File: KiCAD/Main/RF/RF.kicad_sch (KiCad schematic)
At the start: 2 parts

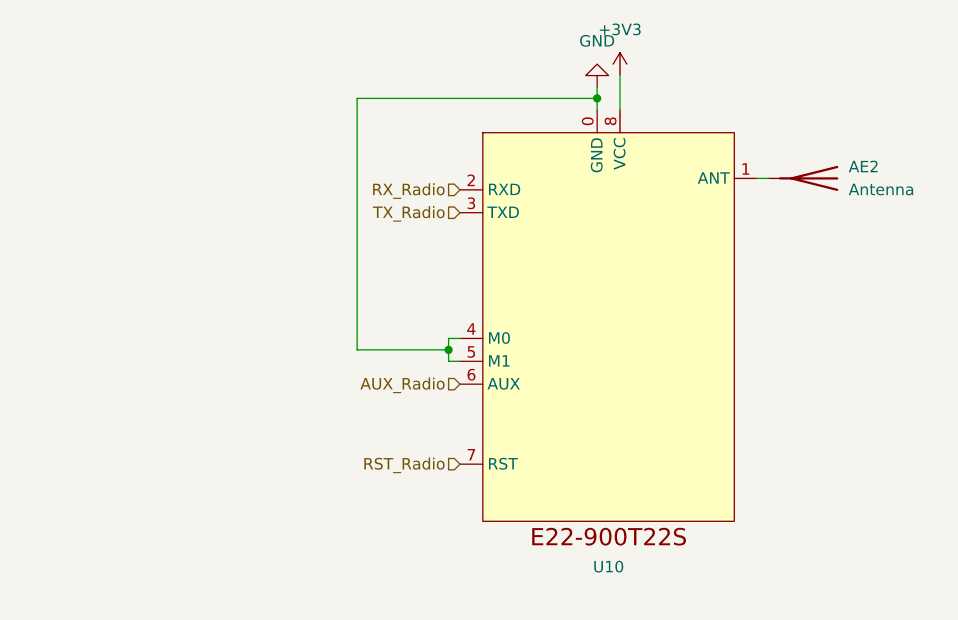
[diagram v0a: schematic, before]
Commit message: Add datasheets and revise TMR goals
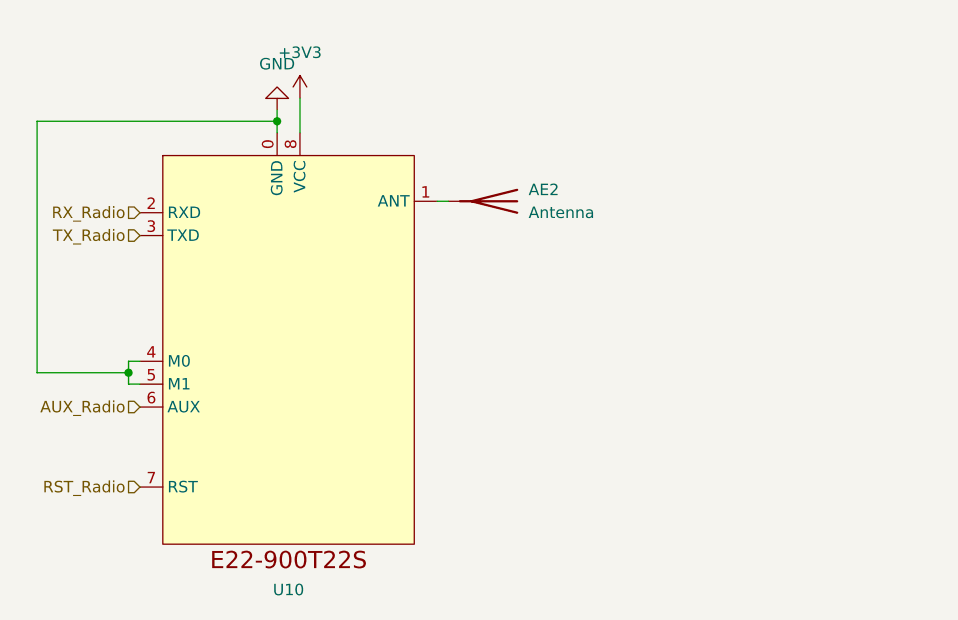
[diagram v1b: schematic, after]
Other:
- company: (none) -> Liquid Rocketry at Illinois Airframe Avionics
- title: (none) -> Ebyte E22 Radio Module
- moved on the sheet: AE2, U10
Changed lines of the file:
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@@
 	(generator_version "9.0")
 	(paper "USLetter")
+	(title_block
+		(title "Ebyte E22 Radio Module")
+		(company "Liquid Rocketry at Illinois Airframe Avionics")
+		(comment 1 "Designed by: Aleph Qin (AE, TMGT Student)")
+	)
 	(junction
-		(at 173.99 76.2)
+		(at 138.43 78.74)
 		(diameter 0)
 		(color 0 0 0 0)
 	)
 	(junction
-		(at 157.48 104.14)
+		(at 121.92 106.68)
 		(diameter 0)
 		(color 0 0 0 0)
@@
 	(wire
 		(pts
-			(xy 158.75 105.41) (xy 157.48 105.41)
-		)
-		(stroke
-			(width 0)
-			(type default)
-		)
-	)
-	(wire
-		(pts
-			(xy 157.48 105.41) (xy 157.48 104.14)
-		)
-		(stroke
-			(width 0)
-			(type default)
-		)
-	)
-	(wire
-		(pts
-			(xy 176.53 73.66) (xy 176.53 77.47)
-		)
-		(stroke
-			(width 0)
-			(type default)
-		)
-	)
-	(wire
-		(pts
-			(xy 147.32 76.2) (xy 147.32 104.14)
-		)
-		(stroke
-			(width 0)
-			(type default)
-		)
-	)
-	(wire
-		(pts
-			(xy 147.32 104.14) (xy 157.48 104.14)
-		)
-		(stroke
-			(width 0)
-			(type default)
-		)
-	)
-	(wire
-		(pts
-			(xy 193.04 85.09) (xy 191.77 85.09)
-		)
-		(stroke
-			(width 0)
-			(type default)
-		)
-	)
-	(wire
-		(pts
-			(xy 173.99 76.2) (xy 147.32 76.2)
-		)
-		(stroke
-			(width 0)
-			(type default)
-		)
-	)
-	(wire
-		(pts
-			(xy 157.48 102.87) (xy 157.48 104.14)
-		)
-		(stroke
-			(width 0)
-			(type default)
-		)
-	)
-	(wire
-		(pts
-			(xy 173.99 76.2) (xy 173.99 77.47)
-		)
-		(stroke
-			(width 0)
-			(type default)
-		)
-	)
-	(wire
-		(pts
-			(xy 173.99 74.93) (xy 173.99 76.2)
-		)
-		(stroke
-			(width 0)
-			(type default)
-		)
-	)
-	(wire
-		(pts
-			(xy 157.48 102.87) (xy 158.75 102.87)
+			(xy 123.19 107.95) (xy 121.92 107.95)
+		)
+		(stroke
+			(width 0)
+			(type default)
+		)
+	)
+	(wire
+		(pts
+			(xy 121.92 107.95) (xy 121.92 106.68)
+		)
+		(stroke
+			(width 0)
+			(type default)
+		)
+	)
+	(wire
+		(pts
+			(xy 140.97 76.2) (xy 140.97 80.01)
+		)
+		(stroke
+			(width 0)
+			(type default)
+		)
+	)
+	(wire
+		(pts
+			(xy 111.76 78.74) (xy 111.76 106.68)
+		)
+		(stroke
+			(width 0)
+			(type default)
+		)
+	)
+	(wire
+		(pts
+			(xy 111.76 106.68) (xy 121.92 106.68)
+		)
+		(stroke
+			(width 0)
+			(type default)
+		)
+	)
+	(wire
+		(pts
+			(xy 157.48 87.63) (xy 156.21 87.63)
+		)
+		(stroke
+			(width 0)
+			(type default)
+		)
+	)
+	(wire
+		(pts
+			(xy 138.43 78.74) (xy 111.76 78.74)
+		)
+		(stroke
+			(width 0)
+			(type default)
+		)
+	)
+	(wire
+		(pts
+			(xy 121.92 105.41) (xy 121.92 106.68)
+		)
+		(stroke
+			(width 0)
+			(type default)
+		)
+	)
+	(wire
+		(pts
+			(xy 138.43 78.74) (xy 138.43 80.01)
+		)
+		(stroke
+			(width 0)
+			(type default)
+		)
+	)
+	(wire
+		(pts
+			(xy 138.43 77.47) (xy 138.43 78.74)
+		)
+		(stroke
+			(width 0)
+			(type default)
+		)
+	)
+	(wire
+		(pts
+			(xy 121.92 105.41) (xy 123.19 105.41)
 		)
 		(stroke
@@
 	(hierarchical_label "TX_Radio"
 		(shape input)
-		(at 158.75 88.9 180)
+		(at 123.19 91.44 180)
 		(effects
 			(font
@@
 	(hierarchical_label "RST_Radio"
 		(shape input)
-		(at 158.75 116.84 180)
+		(at 123.19 119.38 180)
 		(effects
 			(font
@@
 	(hierarchical_label "AUX_Radio"
 		(shape input)
-		(at 158.75 107.95 180)
+		(at 123.19 110.49 180)
 		(effects
 			(font
@@
 	(hierarchical_label "RX_Radio"
 		(shape input)
-		(at 158.75 86.36 180)
+		(at 123.19 88.9 180)
 		(effects
 			(font
@@
 	(symbol
 		(lib_id "power:+3V3")
-		(at 176.53 73.66 0)
+		(at 140.97 76.2 0)
 		(unit 1)
 		(exclude_from_sim no)
@@
 		(fields_autoplaced yes)
 		(property "Reference" "#PWR024"
-			(at 176.53 77.47 0)
+			(at 140.97 80.01 0)
 			(effects
 				(font
@@
 		)
 		(property "Value" "+3V3"
-			(at 176.53 68.58 0)
+			(at 140.97 71.12 0)
 			(effects
 				(font
@@
 		)
 		(property "Footprint" ""
-			(at 176.53 73.66 0)
+			(at 140.97 76.2 0)
 			(effects
 				(font
@@
 		)
 		(property "Datasheet" ""
-			(at 176.53 73.66 0)
+			(at 140.97 76.2 0)
 			(effects
 				(font
@@
 		)
 		(property "Description" "Power symbol creates a global label with name \"+3V3\""
-			(at 176.53 73.66 0)
+			(at 140.97 76.2 0)
 			(effects
 				(font
@@
 	(symbol
 		(lib_id "E22-900T22S:E22-900T22S")
-		(at 175.26 101.6 0)
+		(at 139.7 104.14 0)
 		(unit 1)
 		(exclude_from_sim no)
@@
 		(fields_autoplaced yes)
 		(property "Reference" "U10"
-			(at 175.26 128.27 0)
+			(at 139.7 130.81 0)
 			(effects
 				(font
@@
 		)
 		(property "Value" "~"
-			(at 175.26 130.81 0)
+			(at 139.7 133.35 0)
 			(effects
 				(font
@@
 		)
 		(property "Footprint" ""
-			(at 175.26 101.6 0)
+			(at 139.7 104.14 0)
 			(effects
 				(font
@@
 		)
 		(property "Datasheet" ""
-			(at 175.26 101.6 0)
+			(at 139.7 104.14 0)
 			(effects
 				(font
@@
 		)
 		(property "Description" ""
-			(at 175.26 101.6 0)
+			(at 139.7 104.14 0)
 			(effects
 				(font
@@
 	(symbol
 		(lib_id "power:GND")
-		(at 173.99 74.93 0)
+		(at 138.43 77.47 0)
 		(mirror x)
 		(unit 1)
@@
 		(dnp no)
 		(property "Reference" "#PWR025"
-			(at 173.99 68.58 0)
+			(at 138.43 71.12 0)
 			(effects
 				(font
@@
 		)
 		(property "Value" "GND"
-			(at 173.99 69.85 0)
+			(at 138.43 72.39 0)
 			(effects
 				(font
@@
 		)
 		(property "Footprint" ""
-			(at 173.99 74.93 0)
+			(at 138.43 77.47 0)
 			(effects
 				(font
@@
 		)
 		(property "Datasheet" ""
-			(at 173.99 74.93 0)
+			(at 138.43 77.47 0)
 			(effects
 				(font
@@
 		)
 		(property "Description" "Power symbol creates a global label with name \"GND\" , ground"
-			(at 173.99 74.93 0)
+			(at 138.43 77.47 0)
 			(effects
 				(font
@@
 	(symbol
 		(lib_id "Device:Antenna")
-		(at 198.12 85.09 270)
+		(at 162.56 87.63 270)
 		(unit 1)
 		(exclude_from_sim no)
@@
 		(fields_autoplaced yes)
 		(property "Reference" "AE2"
-			(at 201.93 83.82 90)
+			(at 166.37 86.36 90)
 			(effects
 				(font
@@
 		)
 		(property "Value" "Antenna"
-			(at 201.93 86.36 90)
+			(at 166.37 88.9 90)
 			(effects
 				(font
@@
 		)
 		(property "Footprint" ""
-			(at 198.12 85.09 0)
+			(at 162.56 87.63 0)
 			(effects
 				(font
@@
 		)
 		(property "Datasheet" "~"
-			(at 198.12 85.09 0)
+			(at 162.56 87.63 0)
 			(effects
 				(font
@@
 		)
 		(property "Description" "Antenna"
-			(at 198.12 85.09 0)
-			(effects
-				(font
+			(at 162.56 87.63 0)
+			(effects
+				(font

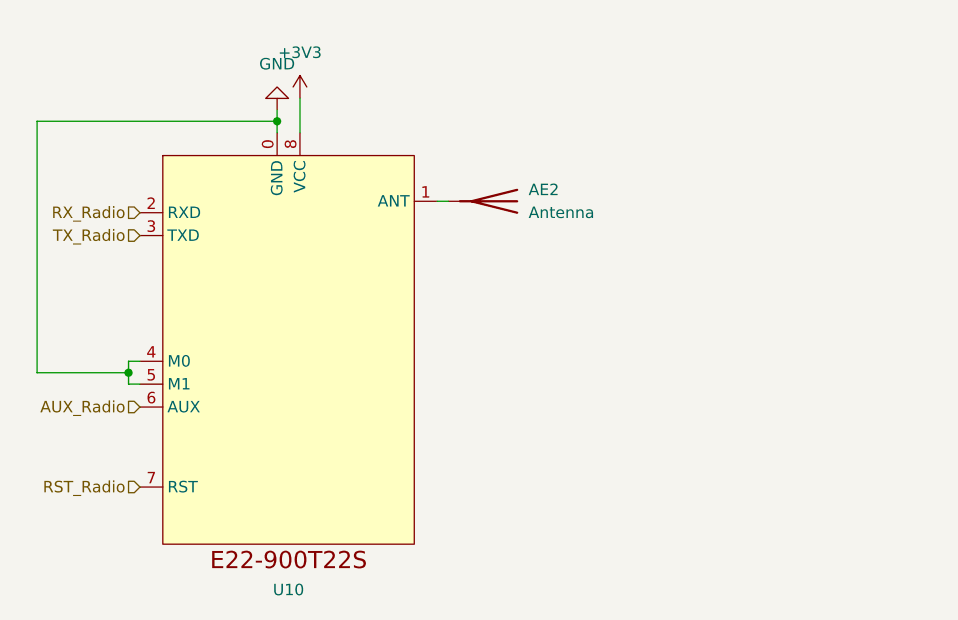
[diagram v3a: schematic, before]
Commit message: Update RF sys and footprints
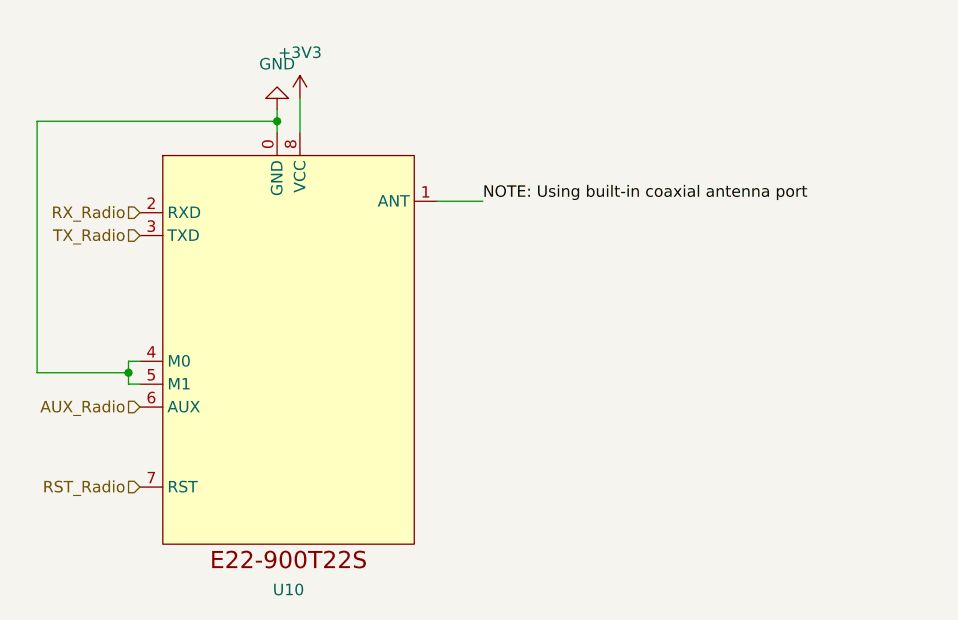
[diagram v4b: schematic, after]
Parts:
- removed AE2: Antenna, symbol Device:Antenna
- U10: footprint (none) -> E22-900M22S:E22-900M22S
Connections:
- net NOTE: Using built-in coaxial antenna port: now reaches U10.1 (ANT)
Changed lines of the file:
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@@
-	(wire
-		(pts
-			(xy 157.48 87.63) (xy 156.21 87.63)
-		)
-		(stroke
-			(width 0)
-			(type default)
-		)
-	)
 	(wire
 		(pts
@@
 	(wire
 		(pts
+			(xy 156.21 87.63) (xy 161.29 87.63)
+		)
+		(stroke
+			(width 0)
+			(type default)
+		)
+	)
+	(wire
+		(pts
 			(xy 138.43 78.74) (xy 138.43 80.01)
 		)
@@
 			(width 0)
 			(type default)
+		)
+	)
+	(label "NOTE: Using built-in coaxial antenna port"
+		(at 161.29 87.63 0)
+		(effects
+			(font
+				(size 1.27 1.27)
+			)
+			(justify left bottom)
 		)
 	)
@@
 			)
 		)
-		(property "Footprint" ""
+		(property "Footprint" "E22-900M22S:E22-900M22S"
 			(at 139.7 104.14 0)
 			(effects
@@
 					(unit 1)
 				)
-			)
-		)
-	)
-	(symbol
-		(lib_id "Device:Antenna")
-		(at 162.56 87.63 270)
-		(unit 1)
-		(exclude_from_sim no)
-		(in_bom yes)
-		(on_board yes)
-		(dnp no)
-		(fields_autoplaced yes)
-		(property "Reference" "AE2"
-			(at 166.37 86.36 90)
-			(effects
-				(font
-					(size 1.27 1.27)
-				)
-				(justify left)
-			)
-		)
-		(property "Value" "Antenna"
-			(at 166.37 88.9 90)
-			(effects
-				(font
-					(size 1.27 1.27)
-				)
-				(justify left)
-			)
-		)
-		(property "Footprint" ""
-			(at 162.56 87.63 0)
-			(effects
-				(font
-					(size 1.27 1.27)
-				)
-				(hide yes)
-			)
-		)
-		(property "Datasheet" "~"
-			(at 162.56 87.63 0)
-			(effects
-				(font
-					(size 1.27 1.27)
-				)
-				(hide yes)
-			)
-		)
-		(property "Description" "Antenna"
-			(at 162.56 87.63 0)
-			(effects
-				(font
-					(size 1.27 1.27)
-				)
-				(hide yes)
-			)
-		)
-		(pin "1"
-		)
-		(instances
-			(project "Main"
-				(path "/bbb10697-a5dd-43b8-9c6f-4c5919cf3463/cea653c8-bb92-4989-ba48-a3585205b361"
-					(reference "AE2")
-					(unit 1)
-				)

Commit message: 30%
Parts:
- added J9: Conn_Coaxial, Connector_Coaxial:U.FL_Molex_MCRF_73412-0110_Vertical, symbol Connector:Conn_Coaxial
- U10: footprint E22-900M22S:E22-900M22S -> E22-900T22S:E22-900T22S
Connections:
- net GND: now also J9.2 (Ext)
- net NOTE: Using built-in coaxial antenna port: no longer names the net of U10.1 (ANT)
- net NOTE: Using built-in coaxial antenna port: now also J9.1 (In)
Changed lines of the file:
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@@
+	(wire
+		(pts
+			(xy 175.26 92.71) (xy 175.26 93.98)
+		)
+		(stroke
+			(width 0)
+			(type default)
+		)
+	)
 	(wire
 		(pts
@@
 	(wire
 		(pts
-			(xy 156.21 87.63) (xy 161.29 87.63)
+			(xy 156.21 87.63) (xy 170.18 87.63)
 		)
 		(stroke
@@
 			(width 0)
 			(type default)
-		)
-	)
-	(label "NOTE: Using built-in coaxial antenna port"
-		(at 161.29 87.63 0)
-		(effects
-			(font
-				(size 1.27 1.27)
-			)
-			(justify left bottom)
 		)
 	)
@@
 			)
 			(justify right)
+		)
+	)
+	(symbol
+		(lib_id "Connector:Conn_Coaxial")
+		(at 175.26 87.63 0)
+		(unit 1)
+		(exclude_from_sim no)
+		(in_bom yes)
+		(on_board yes)
+		(dnp no)
+		(fields_autoplaced yes)
+		(property "Reference" "J9"
+			(at 179.07 86.6531 0)
+			(effects
+				(font
+					(size 1.27 1.27)
+				)
+				(justify left)
+			)
+		)
+		(property "Value" "Conn_Coaxial"
+			(at 179.07 89.1931 0)
+			(effects
+				(font
+					(size 1.27 1.27)
+				)
+				(justify left)
+			)
+		)
+		(property "Footprint" "Connector_Coaxial:U.FL_Molex_MCRF_73412-0110_Vertical"
+			(at 175.26 87.63 0)
+			(effects
+				(font
+					(size 1.27 1.27)
+				)
+				(hide yes)
+			)
+		)
+		(property "Datasheet" "~"
+			(at 175.26 87.63 0)
+			(effects
+				(font
+					(size 1.27 1.27)
+				)
+				(hide yes)
+			)
+		)
+		(property "Description" "coaxial connector (BNC, SMA, SMB, SMC, Cinch/RCA, LEMO, ...)"
+			(at 175.26 87.63 0)
+			(effects
+				(font
+					(size 1.27 1.27)
+				)
+				(hide yes)
+			)
+		)
+		(pin "2"
+		)
+		(pin "1"
+		)
+		(instances
+			(project "Main"
+				(path "/bbb10697-a5dd-43b8-9c6f-4c5919cf3463/cea653c8-bb92-4989-ba48-a3585205b361"
+					(reference "J9")
+					(unit 1)
+				)
+			)
 		)
 	)
@@
 			)
 		)
-		(property "Footprint" "E22-900M22S:E22-900M22S"
+		(property "Footprint" "E22-900T22S:E22-900T22S"
 			(at 139.7 104.14 0)
 			(effects
@@
 					(unit 1)
 				)
+			)
+		)
+	)
+	(symbol
+		(lib_id "power:GND")
+		(at 175.26 93.98 0)
+		(unit 1)
+		(exclude_from_sim no)
+		(in_bom yes)
+		(on_board yes)
+		(dnp no)
+		(fields_autoplaced yes)
+		(property "Reference" "#PWR055"
+			(at 175.26 100.33 0)
+			(effects
+				(font
+					(size 1.27 1.27)
+				)
+				(hide yes)
+			)
+		)
+		(property "Value" "GND"
+			(at 175.26 99.06 0)
+			(effects
+				(font
+					(size 1.27 1.27)
+				)
+			)
+		)
+		(property "Footprint" ""
+			(at 175.26 93.98 0)
+			(effects
+				(font
+					(size 1.27 1.27)
+				)
+				(hide yes)
+			)
+		)
+		(property "Datasheet" ""
+			(at 175.26 93.98 0)
+			(effects
+				(font
+					(size 1.27 1.27)
+				)
+				(hide yes)
+			)
+		)
+		(property "Description" "Power symbol creates a global label with name \"GND\" , ground"
+			(at 175.26 93.98 0)
+			(effects
+				(font
+					(size 1.27 1.27)
+				)
+				(hide yes)
+			)
+		)
+		(pin "1"
+		)
+		(instances
+			(project "Main"
+				(path "/bbb10697-a5dd-43b8-9c6f-4c5919cf3463/cea653c8-bb92-4989-ba48-a3585205b361"
+					(reference "#PWR055")
+					(unit 1)
+				)
